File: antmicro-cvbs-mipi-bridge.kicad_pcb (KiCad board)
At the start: 2 copper layers, 60 x 60 mm, 62 parts, among them IC1 MIPI 10Bit 4x Oversampled SDT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, IC2 LDO 1.8V 250mA, IC3 IC, LDO, REG, 3.3V, SOT223, IC4 Single Schmitt trigger buffer, IC5 Single Schmitt trigger buffer, J1 MODULAR, JACK, THT, R/A, RJ45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, J7 1x2 pinhead male, Q1 20 V, dual N-channel Trench M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, Y1 TXC 7B-28.63636MAAJ-T XTAL, 2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

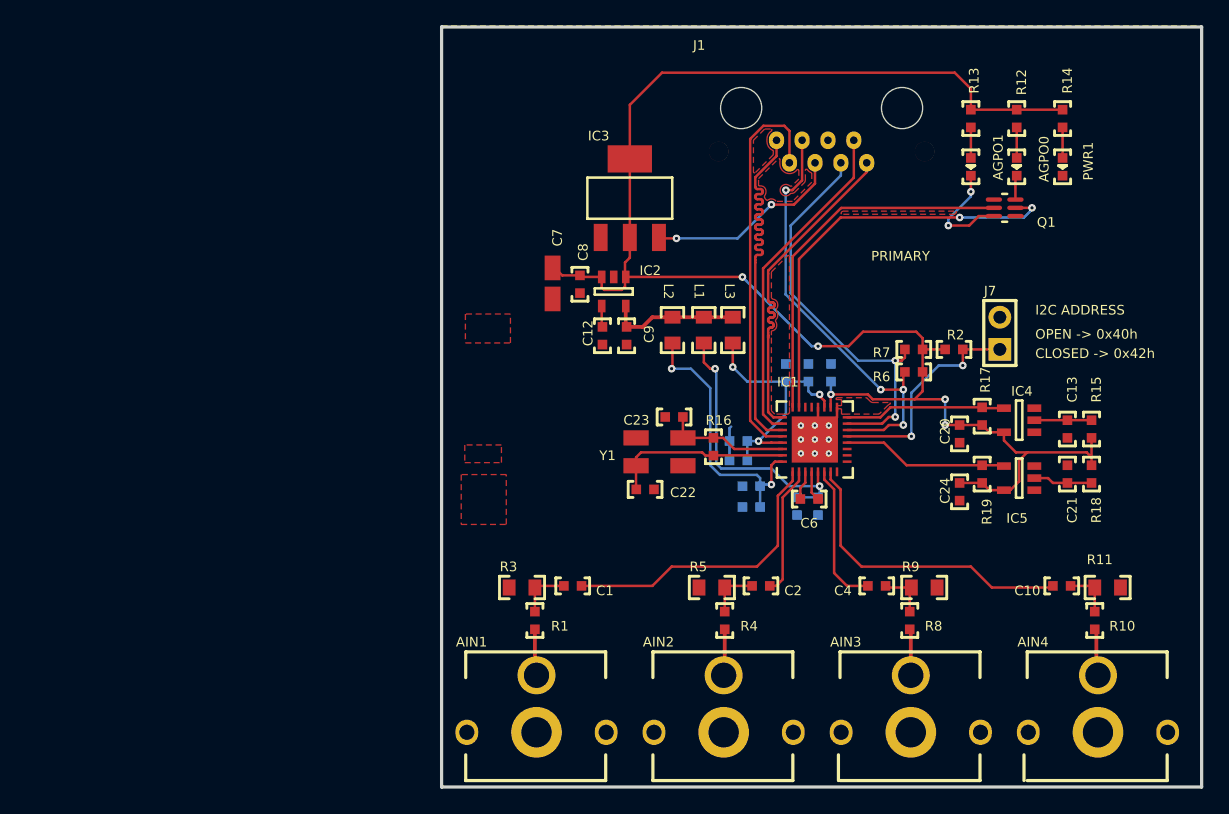
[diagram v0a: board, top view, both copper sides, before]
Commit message: Started component positions adjusment and placement
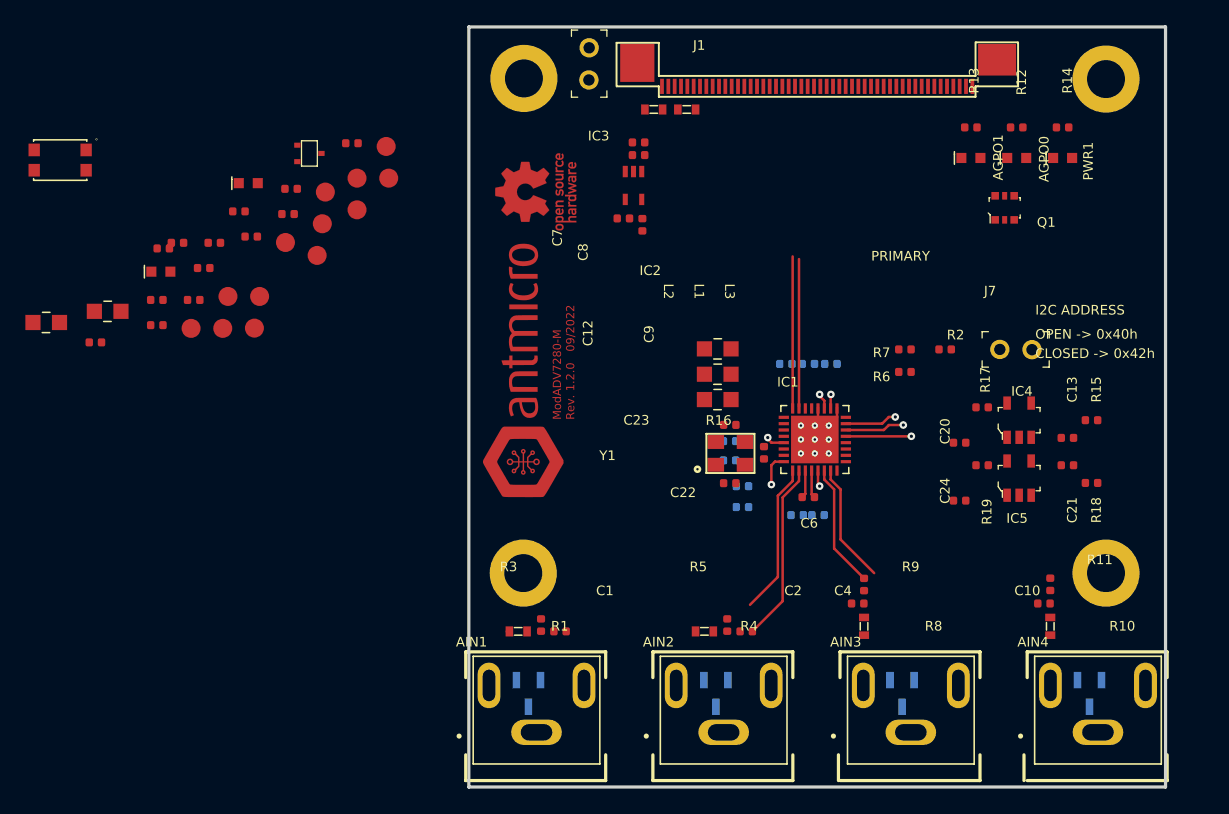
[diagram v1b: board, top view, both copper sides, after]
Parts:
- removed IC3: IC, LDO, REG, 3.3V, SOT223, SOT223
- removed L1, L2, L3: WURTH ELEKTRONIK - 742792022 - FERRITE BEAD, 0.05OHM, 2A, 0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, 0805
- added C25: C_1u_0603, antmicro-footprints:0603-cap, F.Cu at (126.3, 62.4)
- added C26: C_100n_0402, antmicro-footprints:0402-cap, F.Cu at (88.7, 72.9)
- added C27: C_1u_0402, antmicro-footprints:0402-cap, F.Cu at (102.5, 65.1)
- added C28: C_1u_0402, antmicro-footprints:0402-cap, F.Cu at (97.4, 70.7)
- added D1: PESD1CAN_215, antmicro-footprints:SOT-23-3, B.Cu at (116.4, 108.5)
- added D2: PESD1CAN_215, antmicro-footprints:SOT-23-3, B.Cu at (131.2, 108.5)
- added D3: PESD1CAN_215, antmicro-footprints:SOT-23-3, B.Cu at (145.9, 108.5)
- added D4: PESD1CAN_215, antmicro-footprints:SOT-23-3, B.Cu at (160.7, 108.5)
- added FB1: 742792022, antmicro-footprints:0805-res, F.Cu at (83.2, 78.3)
- added FB2: 742792022, antmicro-footprints:0805-res, F.Cu at (78.3, 79.2)
- added FB3: 742792022, antmicro-footprints:0805-res, F.Cu at (131.3, 81.3)
- added FB4: 742792022, antmicro-footprints:0805-res, F.Cu at (131.3, 83.3)
- added FB5: 742792022, antmicro-footprints:0805-res, F.Cu at (131.3, 85.3)
- added J2: 61300211121, antmicro-footprints:PinHeader_1x2_P2.54_Drill0.9mm, F.Cu at (121.2, 57.5)
- added MP1: 9774030243R, antmicro-footprints:9774030243R, F.Cu at (116.0, 60.0)
- added MP2: 9774030243R, antmicro-footprints:9774030243R, F.Cu at (116.0, 99.0)
- added MP3: 9774030243R, antmicro-footprints:9774030243R, F.Cu at (161.9, 60.0)
- added MP4: 9774030243R, antmicro-footprints:9774030243R, F.Cu at (161.9, 99.0)
- added N1: antmicro_logo, antmicro-footprints:antmicro-logo_scaled_20mm, F.Cu at (116.2, 83.0)
- added N2: oshw_logo, antmicro-footprints:oshw-logo, F.Cu at (117.0, 68.9)
- added PWR2: KP-1608ZGC, antmicro-footprints:LED_0603, F.Cu at (94.3, 68.2)
- added PWR3: KP-1608ZGC, antmicro-footprints:LED_0603, F.Cu at (87.4, 75.2)
- added Q2: BSS138APW, antmicro-footprints:SC70-3, F.Cu at (99.1, 65.9)
- added R20: R_0R_0402, antmicro-footprints:0402-res, F.Cu at (94.5, 72.4)
- added R21: R_0R_0402, antmicro-footprints:0402-res, F.Cu at (87.1, 77.4)
- added R22: R_0R_0402, antmicro-footprints:0402-res, F.Cu at (82.2, 80.8)
- added R23: R_0R_0402, antmicro-footprints:0402-res, F.Cu at (91.6, 72.9)
- added R24: R_0R_0402, antmicro-footprints:0402-res, F.Cu at (97.7, 68.7)
- added R25: R_0R_0402, antmicro-footprints:0402-res, F.Cu at (90.8, 74.9)
- added R26: R_470R_0402, antmicro-footprints:0402-res, F.Cu at (87.6, 73.4)
- added R27: R_1k_0402, antmicro-footprints:0402-res, F.Cu at (90.0, 77.4)
- added R28: R_100k_0402, antmicro-footprints:0402-res, F.Cu at (87.1, 79.4)
- added R29: R_1k_0402, antmicro-footprints:0402-res, F.Cu at (93.5, 70.4)
- added R30: R_0R_0402, antmicro-footprints:0402-res, F.Cu at (125.4, 71.5)
- added S1: KMR2, antmicro-footprints:SW_SPST_4.2x2.8, F.Cu at (79.4, 66.4)
- added TP1: TP, antmicro-footprints:TP-R-1.5, F.Cu at (102.9, 67.8)
- added TP10: TP, antmicro-footprints:TP-R-1.5, F.Cu at (105.2, 65.3)
- added TP11: TP, antmicro-footprints:TP-R-1.5, F.Cu at (92.7, 77.2)
- added TP12: TP, antmicro-footprints:TP-R-1.5, F.Cu at (89.8, 79.7)
- added TP13: TP, antmicro-footprints:TP-R-1.5, F.Cu at (105.4, 67.8)
- added TP2: TP, antmicro-footprints:TP-R-1.5, F.Cu at (97.2, 72.9)
- added TP3: TP, antmicro-footprints:TP-R-1.5, F.Cu at (99.7, 73.9)
- added TP4: TP, antmicro-footprints:TP-R-1.5, F.Cu at (100.4, 68.9)
- added TP5: TP, antmicro-footprints:TP-R-1.5, F.Cu at (102.9, 70.3)
- added TP6: TP, antmicro-footprints:TP-R-1.5, F.Cu at (94.8, 79.7)
- added TP7: TP, antmicro-footprints:TP-R-1.5, F.Cu at (95.2, 77.2)
- added TP8: TP, antmicro-footprints:TP-R-1.5, F.Cu at (100.1, 71.4)
- added TP9: TP, antmicro-footprints:TP-R-1.5, F.Cu at (92.3, 79.7)
- AGPO0, AGPO1, PWR1: value LED Green 0603 case -> KP-1608ZGC; footprint LED0603 -> antmicro-footprints:LED_0603
- AIN1, AIN2, AIN3, AIN4: value Shielded RCA socket -> PJRAN1X1U01X; footprint CC-134B -> antmicro-footprints:PJRAN1X1U01X
- C1, C10, C13, C14, C16, C17, C2, C20, C21, C24, C3, C4, C5, C6: value MLCC SMT Capacitor 100nF 0603 -> C_100n_0402; footprint 0603 -> antmicro-footprints:0402-cap
- C11, C15, C18, C19: value MLCC SMT Capacitor 10nF 0603 -> C_10n_0402; footprint 0603 -> antmicro-footprints:0402-cap
- C12: value MLCC SMT Capacitor 10nF 0603 -> C_1u_0603; footprint 0603 -> antmicro-footprints:0603-cap
- C22, C23: value MLCC SMT Capacitor 27pF 0603 -> C_10p_0402; footprint 0603 -> antmicro-footprints:0402-cap
- C7: value Tantalum SMT Capacitor 100uF Case KEMET_A -> C_100n_0402; footprint KEMET_A -> antmicro-footprints:0402-cap
- C8, C9: value MLCC SMT Capacitor 10uF 0603 -> C_1u_0402; footprint 0603 -> antmicro-footprints:0402-cap
- IC1: value MIPI 10Bit 4x Oversampled SDTV Video Decoder with Deinterlacer -> ADV7280BCPZ-M; footprint LFCSP-32 -> antmicro-footprints:LFCSP-32-1EP-5x5mm
- IC2: value LDO 1.8V 250mA -> TLV70018; footprint SOT23-5N -> antmicro-footprints:SC-70-5
- IC4, IC5: value Single Schmitt trigger buffer -> SN74AUP1G17DCKR; footprint SOT23127P600-8N -> antmicro-footprints:SOT-753
- J1: value MODULAR, JACK, THT, R/A, RJ45, 8P8C -> WE_68715014522_ONE-SIDE; footprint RJ45 AMP-1-406541 -> antmicro-footprints:WE_68715014522_ONE-SIDE
- J7: value 1x2 pinhead male -> 61300211121; footprint HEADER_1X2_male 2.54mm -> antmicro-footprints:PinHeader_1x2_P2.54_Drill0.9mm
- Q1: value 20 V, dual N-channel Trench MOSFET -> NX3008NBKS_2; footprint TSOP65P210X110-6N -> antmicro-footprints:SOT-363
- R1, R10, R4, R8: value SMT Resistor 24R 0603 -> R_24R_0603; footprint 0603 -> antmicro-footprints:0603-res
- R11, R3, R5, R9: value SMT Resistor 51R 0805 -> R_51R_0402; footprint 0805 -> antmicro-footprints:0402-res
- R12, R13, R14: value SMT Resistor 330R 0603 -> R_470R_0402; footprint 0603 -> antmicro-footprints:0402-res
- R15: value SMT Resistor 22k 0603 -> R_22k_0402; footprint 0603 -> antmicro-footprints:0402-res
- R16: value SMT Resistor 1M 0603 -> R_1M0_0402; footprint 0603 -> antmicro-footprints:0402-res
- R17, R18, R19: value SMT Resistor 100k 0603 -> R_100k_0402; footprint 0603 -> antmicro-footprints:0402-res
- R2: value SMT Resistor 1k 0603 -> R_1k_0402; footprint 0603 -> antmicro-footprints:0402-res
- R6, R7: value SMT Resistor 4k7 0603 -> R_4k7_0402; footprint 0603 -> antmicro-footprints:0402-res
- Y1: value TXC 7B-28.63636MAAJ-T XTAL, 28.63636MHZ, 18PF, SMD, 5X3.2 -> ABM8G-28.63636MHZ-18-D2Y-T; footprint TXC_7B -> antmicro-footprints:KX-7
- moved C12 19.7 mm to (128.9, 62.4)
- moved C8 12.8 mm to (125.1, 65.0), turned to 180 degrees
- moved C7 12.2 mm to (125.1, 66.0)
- moved C9 9.96 mm to (123.9, 71.0), turned to 180 degrees
- moved IC2 8.51 mm to (124.7, 68.4), turned to 180 degrees
- moved J1 6.69 mm to (139.2, 61.2), turned to 180 degrees
- moved R9 6.39 mm to (142.4, 101.4)
- moved R11 6.17 mm to (157.1, 101.4)
- moved C22 6.01 mm to (132.3, 91.9)
- moved C23 5.14 mm to (132.3, 87.3), turned to 180 degrees
- moved R16 3.99 mm to (135.0, 89.5), turned to 90 degrees
- moved R3 3.89 mm to (117.4, 103.1), turned to -90 degrees
- moved Y1 3.88 mm to (132.3, 89.5)
- moved R5 3.71 mm to (132.1, 103.1), turned to -90 degrees
- moved C2 3.62 mm to (133.6, 103.6)
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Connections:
- C1 pad 1: (no net) -> Net-(C1-Pad1)
- C1 pad 2: (no net) -> /AIN1
- C10 pad 1: (no net) -> Net-(C10-Pad1)
- C10 pad 2: (no net) -> /AIN4
- C11 pad 1: (no net) -> PVDD_1V8
- C11 pad 2: (no net) -> GND
- C12 pad 1: (no net) -> Net-(C12-Pad1)
- C12 pad 2: (no net) -> GND
- C13 pad 1: (no net) -> Net-(C13-Pad1)
- C13 pad 2: (no net) -> GND
- C14 pad 1: (no net) -> GND
- C14 pad 2: (no net) -> AVDD_1V8
- C15 pad 1: (no net) -> AVDD_1V8
- C15 pad 2: (no net) -> GND
- C16 pad 1: (no net) -> GND
- C16 pad 2: (no net) -> DVDD_1V8
- C17 pad 1: (no net) -> GND
- C17 pad 2: (no net) -> DVDD_1V8
- C18 pad 1: (no net) -> DVDD_1V8
- C18 pad 2: (no net) -> GND
- C19 pad 1: (no net) -> DVDD_1V8
- C19 pad 2: (no net) -> GND
- C2 pad 1: (no net) -> Net-(C2-Pad1)
- C2 pad 2: (no net) -> /AIN2
- C20 pad 1: (no net) -> 3V3_SYS
- C20 pad 2: (no net) -> GND
- C21 pad 1: (no net) -> Net-(C21-Pad1)
- C21 pad 2: (no net) -> GND
- C22 pad 1: (no net) -> /XTAL_N
- C22 pad 2: (no net) -> GND
- C23 pad 1: (no net) -> /XTAL_P
- C23 pad 2: (no net) -> GND
- C24 pad 1: (no net) -> 3V3_SYS
- C24 pad 2: (no net) -> GND
- C3 pad 1: (no net) -> GND
- C3 pad 2: (no net) -> PVDD_1V8
- C4 pad 1: (no net) -> Net-(C4-Pad1)
- C4 pad 2: (no net) -> /AIN3
- C5 pad 1: (no net) -> GND
- C5 pad 2: (no net) -> 3V3_SYS
- C6 pad 1: (no net) -> /VREFN
- C6 pad 2: (no net) -> /VREFP
- C7 pad 1: (no net) -> GND
- C7 pad 2: (no net) -> 3V3_SYS
- C8 pad 1: (no net) -> 3V3_SYS
- C8 pad 2: (no net) -> GND
- C9 pad 1: (no net) -> Net-(C9-Pad1)
- C9 pad 2: (no net) -> GND
- IC1 pad 1: (no net) -> GND
- IC1 pad 10: (no net) -> /CSI_A_D0_N
- IC1 pad 11: (no net) -> /CSI_A_CLK_P
- IC1 pad 12: (no net) -> /CSI_A_CLK_N
- IC1 pad 13: (no net) -> DVDD_1V8
- IC1 pad 14: (no net) -> /XTAL_P
- IC1 pad 15: (no net) -> /XTAL_N
- IC1 pad 16: (no net) -> AVDD_1V8
- IC1 pad 17: (no net) -> /AIN1
- IC1 pad 18: (no net) -> /AIN2
- IC1 pad 19: (no net) -> /VREFP
- IC1 pad 2: (no net) -> 3V3_SYS
- IC1 pad 20: (no net) -> /VREFN
- IC1 pad 21: (no net) -> PVDD_1V8
- IC1 pad 22: (no net) -> /AIN3
- IC1 pad 23: (no net) -> /AIN4
- IC1 pad 24: (no net) -> unconnected-(IC1-Pad24)
- IC1 pad 25: (no net) -> unconnected-(IC1-Pad25)
- IC1 pad 26: (no net) -> unconnected-(IC1-Pad26)
- IC1 pad 27: (no net) -> unconnected-(IC1-Pad27)
- IC1 pad 28: (no net) -> /RESET
- IC1 pad 29: (no net) -> /ALSB
- IC1 pad 3: (no net) -> DVDD_1V8
- IC1 pad 30: (no net) -> /SDA
- IC1 pad 31: (no net) -> /SCL
- IC1 pad 32: (no net) -> /PWRDWN
- IC1 pad 33: (no net) -> GND
- IC1 pad 4: (no net) -> GND
- IC1 pad 5: (no net) -> Net-(IC1-Pad5)
- IC1 pad 6: (no net) -> Net-(IC1-Pad6)
- IC1 pad 7: (no net) -> /AGPO1
- IC1 pad 8: (no net) -> /AGPO0
- IC1 pad 9: (no net) -> /CSI_A_D0_P
- IC2 pad 1: (no net) -> 3V3_SYS
- IC2 pad 2: (no net) -> GND
- IC2 pad 3: (no net) -> 3V3_SYS
- IC2 pad 4: (no net) -> unconnected-(IC2-Pad4)
- IC4 pad 1: (no net) -> unconnected-(IC4-Pad1)
- IC4 pad 2: (no net) -> Net-(C13-Pad1)
- IC4 pad 3: (no net) -> GND
- IC4 pad 4: (no net) -> /PWRDWN
- IC4 pad 5: (no net) -> 3V3_SYS
- IC5 pad 1: (no net) -> unconnected-(IC5-Pad1)
- IC5 pad 2: (no net) -> Net-(C21-Pad1)
- IC5 pad 3: (no net) -> GND
- IC5 pad 4: (no net) -> /RESET
- IC5 pad 5: (no net) -> 3V3_SYS
- J1 pad 1: (no net) -> unconnected-(J1-Pad1)
- J1 pad 2: (no net) -> unconnected-(J1-Pad2)
- J1 pad 3: (no net) -> unconnected-(J1-Pad3)
- J1 pad 4: (no net) -> unconnected-(J1-Pad4)
- J1 pad 5: (no net) -> unconnected-(J1-Pad5)
- J1 pad 6: (no net) -> unconnected-(J1-Pad6)
- J1 pad 7: (no net) -> unconnected-(J1-Pad7)
- J1 pad 8: (no net) -> unconnected-(J1-Pad8)
- J7 pad 1: (no net) -> /ALSB
- J7 pad 2: (no net) -> GND
- Q1 pad 1: (no net) -> GND
- Q1 pad 2: (no net) -> /AGPO0
- Q1 pad 3: (no net) -> Net-(AGPO1-Pad2)
- Q1 pad 4: (no net) -> GND
- Q1 pad 5: (no net) -> /AGPO1
- Q1 pad 6: (no net) -> Net-(AGPO0-Pad2)
- R1 pad 1: (no net) -> /AIN1_ESD
- R1 pad 2: (no net) -> Net-(C1-Pad1)
- R10 pad 1: (no net) -> /AIN4_ESD
- R10 pad 2: (no net) -> Net-(C10-Pad1)
- R11 pad 1: (no net) -> GND
- R11 pad 2: (no net) -> Net-(C10-Pad1)
- R12 pad 1: (no net) -> Net-(AGPO0-Pad1)
- R12 pad 2: (no net) -> 3V3_SYS
- R13 pad 1: (no net) -> Net-(AGPO1-Pad1)
- R13 pad 2: (no net) -> 3V3_SYS
- R14 pad 1: (no net) -> 3V3_SYS
- R14 pad 2: (no net) -> Net-(PWR2-Pad1)
- R15 pad 1: (no net) -> Net-(C13-Pad1)
- R15 pad 2: (no net) -> 3V3_SYS
- R16 pad 1: (no net) -> /XTAL_N
- R16 pad 2: (no net) -> /XTAL_P
- R17 pad 1: (no net) -> /PWRDWN
- R17 pad 2: (no net) -> 3V3_SYS
- R18 pad 1: (no net) -> Net-(C21-Pad1)
- R18 pad 2: (no net) -> 3V3_SYS
- R19 pad 1: (no net) -> /RESET
- R19 pad 2: (no net) -> 3V3_SYS
- R2 pad 1: (no net) -> 3V3_SYS
- R2 pad 2: (no net) -> /ALSB
- R3 pad 1: (no net) -> GND
- R3 pad 2: (no net) -> Net-(C1-Pad1)
- R4 pad 1: (no net) -> /AIN2_ESD
- R4 pad 2: (no net) -> Net-(C2-Pad1)
- R5 pad 1: (no net) -> GND
- R5 pad 2: (no net) -> Net-(C2-Pad1)
- R6 pad 1: (no net) -> /SDA
- R6 pad 2: (no net) -> 3V3_SYS
- R7 pad 1: (no net) -> /SCL
- R7 pad 2: (no net) -> 3V3_SYS
- R8 pad 1: (no net) -> /AIN3_ESD
- R8 pad 2: (no net) -> Net-(C4-Pad1)
- R9 pad 1: (no net) -> GND
- R9 pad 2: (no net) -> Net-(C4-Pad1)
- Y1 pad 1: (no net) -> /XTAL_N
- Y1 pad 2: (no net) -> GND
- Y1 pad 3: (no net) -> /XTAL_P
- Y1 pad 4: (no net) -> GND
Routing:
- net (no net): track 675.1 -> 0.00 mm, vias 35 -> 0
- net /AIN2: track 0.00 -> 14.1 mm
- net /AGPO0: track 0.00 -> 11.9 mm
- net /AIN1: track 0.00 -> 11.9 mm
- net /AGPO1: track 0.00 -> 11.7 mm
- net /AIN3: track 0.00 -> 9.71 mm
- net /AIN4: track 0.00 -> 9.42 mm
- net GND: track 0.00 -> 5.89 mm, vias 0 -> 9
- net /ALSB: track 0.00 -> 5.07 mm, vias 0 -> 1
- net /SDA: track 0.00 -> 4.60 mm, vias 0 -> 1
- net /SCL: track 0.00 -> 4.02 mm, vias 0 -> 1
- net DVDD_1V8: track 0.00 -> 2.56 mm, vias 0 -> 2
- net AVDD_1V8: track 0.00 -> 2.52 mm, vias 0 -> 1
- net /VREFP: track 0.00 -> 2.10 mm
- net /VREFN: track 0.00 -> 2.09 mm
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- removed copper zone on B.Cu, net (none)
- removed copper zone on F.Cu, net (none)
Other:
- board size 60 x 60 mm -> 55 x 60 mm
- copper layers 2 -> 4
- board text added: "${TITLE} Rev. ${REVISION} 09/2022"
- board text added: "0.018 mm"
- board text added: "0.02 mm"
- board text added: "0.035 mm"
- board text added: "0.12 mm"
- board text added: "1"
- board text added: "1.2 mm"
- board text added: "2"
- board text added: "3"
- board text added: "3.5"
- board text added: "4"
- board text added: "4.2"
- board text added: "5"
- board text added: "6"
- board text added: "7"
- board text added: "8"
- board text added: "9"
- board text added: "Bottom Layer"
- board text added: "Bottom Solder"
- board text added: "Constant"
- board text added: "Copper"
- board text added: "Dielectric 1"
- board text added: "Dielectric 2"
- board text added: "Dielectric 3"
- board text added: "FR-4"
- board text added: "Gold plating (ENIG, selective)"
- board text added: "Layer"
- board text added: "Material"
- board text added: "Name"
- board text added: "Power Plane 1"
- board text added: "Power Plane 2"
- board text added: "Prepreg"
- board text added: "Recommended PCB finish:"
- board text added: "Recommended PCB stackup"
- board text added: "Silkscreen: white"
- board text added: "Solder Resist"
- board text added: "Solder mask: matt black"
- board text added: "Suggested prepreg material is ISOLA PR2116"
- board text added: "The design includes high speed signaling"
- board text added: "Thickness"
- board text added: "Top Layer"
- board text added: "Top Solder"
- board text removed: "ModADV7280-M"
- board text removed: "Rev.2.0 06/2015"

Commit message: Finished placement. Removed 5V net and components. Started routing
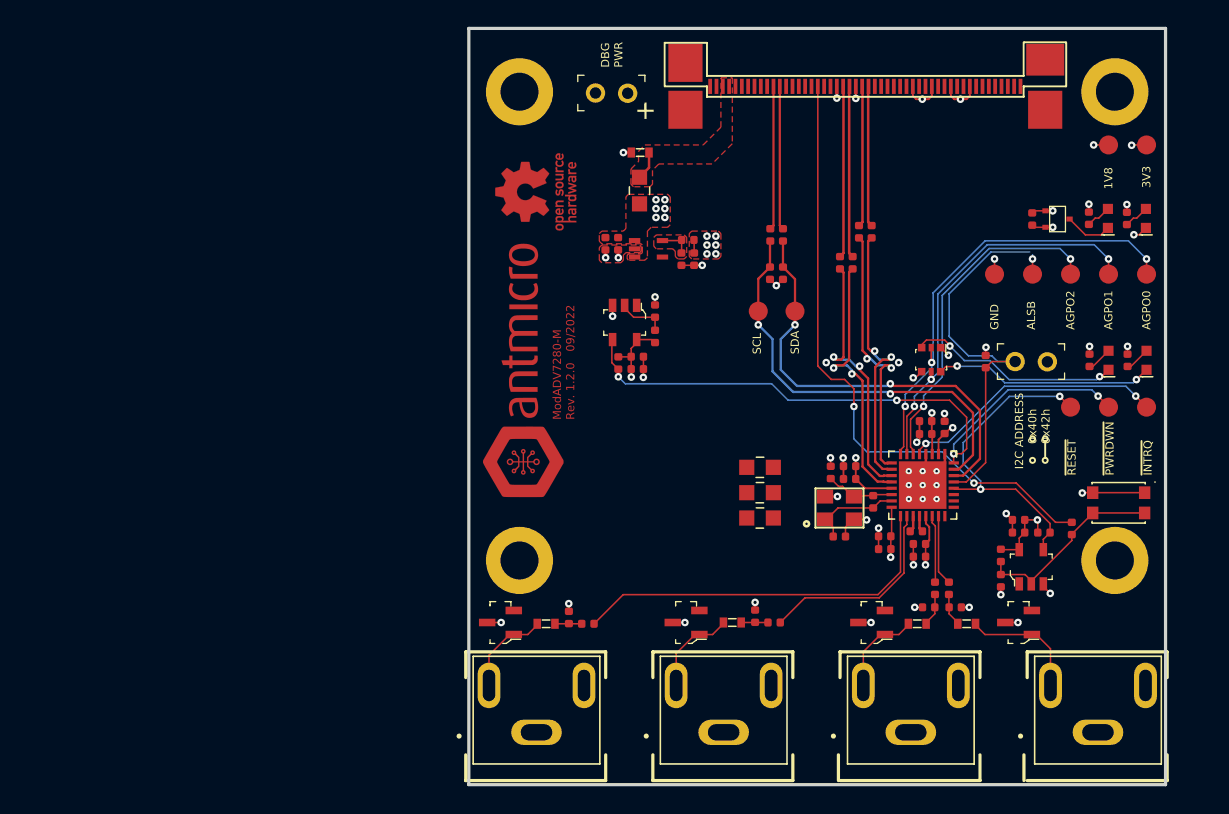
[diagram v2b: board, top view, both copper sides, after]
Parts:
- removed C25: C_1u_0603, antmicro-footprints:0603-cap
- removed FB2: 742792022, antmicro-footprints:0805-res
- removed PWR1: KP-1608ZGC, antmicro-footprints:LED_0603
- removed R27: R_1k_0402, antmicro-footprints:0402-res
- removed TP4: TP, antmicro-footprints:TP-R-1.5
- C11, C14, C15, C16, C17, C18, C19, C3, C5, D1, D2, D3, D4: moved to F.Cu
- J1: value WE_68715014522_ONE-SIDE -> WE_68715014522; footprint antmicro-footprints:WE_68715014522_ONE-SIDE -> antmicro-footprints:WE_68715014522
- MP1, MP2, MP3, MP4: moved to B.Cu
- moved S1 87.8 mm to (163.0, 93.5)
- moved D5 74.9 mm to (162.2, 71.0), turned to 90 degrees
- moved R26 73.1 mm to (160.7, 71.0), turned to -90 degrees
- moved TP11 72.5 mm to (165.2, 75.4), turned to 90 degrees
- moved D6 70.9 mm to (165.2, 71.0), turned to 90 degrees
- moved R29 70.4 mm to (159.3, 95.5), turned to -90 degrees
- moved TP9 70.2 mm to (162.2, 85.9), turned to 180 degrees
- moved R28 69.6 mm to (156.2, 71.0), turned to 90 degrees
- moved TP2 69.2 mm to (165.2, 85.9), turned to 180 degrees
- moved TP12 66.6 mm to (156.2, 75.4)
- moved TP3 63.1 mm to (162.2, 65.2)
- moved C28 62.9 mm to (155.1, 95.8), turned to 180 degrees
- moved TP5 62.5 mm to (165.2, 65.2)
- moved R22 61.9 mm to (143.5, 72.0), turned to 90 degrees
- moved TP8 60.8 mm to (159.2, 85.9), turned to 180 degrees
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- renumbered PWR3 to D5, PWR2 to D6
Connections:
- net Net-(J1-Pad25) renamed /CSI_A_D0_R_N
- net Net-(J1-Pad26) renamed /CSI_A_D0_R_P
- net Net-(J1-Pad28) renamed /CSI_A_CLK_R_N
- net Net-(J1-Pad29) renamed /CSI_A_CLK_R_P
- J1 pad 49: Net-(C25-Pad1) -> unconnected-(J1-Pad49)
- J1 pad 50: Net-(C25-Pad1) -> unconnected-(J1-Pad50)
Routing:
- net /PWRDWN: track 0.00 -> 51.8 mm, vias 0 -> 4
- net /RST_IN: track 0.00 -> 49.6 mm, vias 0 -> 2
- net GND: track 5.89 -> 53.1 mm, vias 9 -> 47
- net /SDA: track 4.60 -> 34.7 mm, vias 1 -> 2
- net /SCL: track 4.02 -> 33.8 mm, vias 1 -> 2
- net Net-(IC1-Pad6): track 0.00 -> 26.8 mm, vias 0 -> 2
- net /ALSB: track 5.07 -> 31.8 mm
- net /RESET: track 0.00 -> 25.6 mm, vias 0 -> 2
- net /AGPO0: track 11.9 -> 35.3 mm, vias 0 -> 3
- net /CSI_A_D0_N: track 0.00 -> 21.9 mm, vias 0 -> 2
- net /CSI_A_CLK_N: track 0.00 -> 21.7 mm, vias 0 -> 2
- net /CSI_A_D0_P: track 0.00 -> 21.2 mm, vias 0 -> 2
- net Net-(IC1-Pad5): track 0.00 -> 21.0 mm, vias 0 -> 2
- net /CSI_A_CLK_P: track 0.00 -> 21.0 mm, vias 0 -> 2
- net /AGPO1: track 11.7 -> 31.0 mm, vias 0 -> 3
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- added copper zone on F.Cu, net 1V8_SYS
- added copper zone on F.Cu, net 3V3_SYS
- added copper zone on In2.Cu, net 3V3_SYS
- added copper zone on F.Cu, net GND
- added copper zone on In1.Cu, net GND
- added copper zone on F.Cu, net Net-(C12-Pad1)
- added copper zone on F.Cu, net Net-(C9-Pad1)
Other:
- board size 55 x 60 mm -> 55 x 59.7 mm
- board text added: "+"
- board text added: "1V8"
- board text added: "3V3"
- board text added: "AGPO2"
- board text added: "ALSB"
- board text added: "DBG PWR"
- board text added: "GND"
- board text added: "I2C ADDRESS 0x40h 0x42h"
- board text added: "SCL"
- board text added: "SDA"
- board text added: "~{INTRQ}"
- board text added: "~{PWRDWN}"
- board text added: "~{RESET}"
- board text removed: "AIN1"
- board text removed: "AIN2"
- board text removed: "AIN3"
- board text removed: "AIN4"
- board text removed: "C1"
- board text removed: "C10"
- board text removed: "C11"
- board text removed: "C12"
- board text removed: "C13"
- board text removed: "C14"
- board text removed: "C15"
- board text removed: "C16"
- board text removed: "C17"
- board text removed: "C18"
- board text removed: "C19"
- board text removed: "C2"
- board text removed: "C20"
- board text removed: "C21"
- board text removed: "C22"
- board text removed: "C23"
- board text removed: "C24"
- board text removed: "C3"
- board text removed: "C4"
- board text removed: "C5"
- board text removed: "C6"
- board text removed: "C7"
- board text removed: "C8"
- board text removed: "C9"
- board text removed: "CLOSED -> 0x42h"
- board text removed: "I2C ADDRESS"
- board text removed: "IC1"
- board text removed: "IC2"
- board text removed: "IC3"
- board text removed: "IC4"
- board text removed: "IC5"
- board text removed: "J1"
- board text removed: "J7"
- board text removed: "L1"
- board text removed: "L2"
- board text removed: "L3"
- board text removed: "OPEN -> 0x40h"
- board text removed: "PRIMARY"
- board text removed: "PWR1"
- board text removed: "Q1"
- board text removed: "R1"
- board text removed: "R10"
- board text removed: "R11"
- board text removed: "R12"
- board text removed: "R13"
- board text removed: "R14"
- board text removed: "R15"
- board text removed: "R16"
- board text removed: "R17"
- board text removed: "R18"
- board text removed: "R19"
- board text removed: "R2"
- board text removed: "R3"
- board text removed: "R4"
- board text removed: "R5"
- board text removed: "R6"
- board text removed: "R7"
- board text removed: "R8"
- board text removed: "R9"
- board text removed: "Y1"
